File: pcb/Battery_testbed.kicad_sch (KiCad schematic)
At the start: 12 parts, among them U5 MIC5504-3.3YM5, U6 MCP73831-2-OT

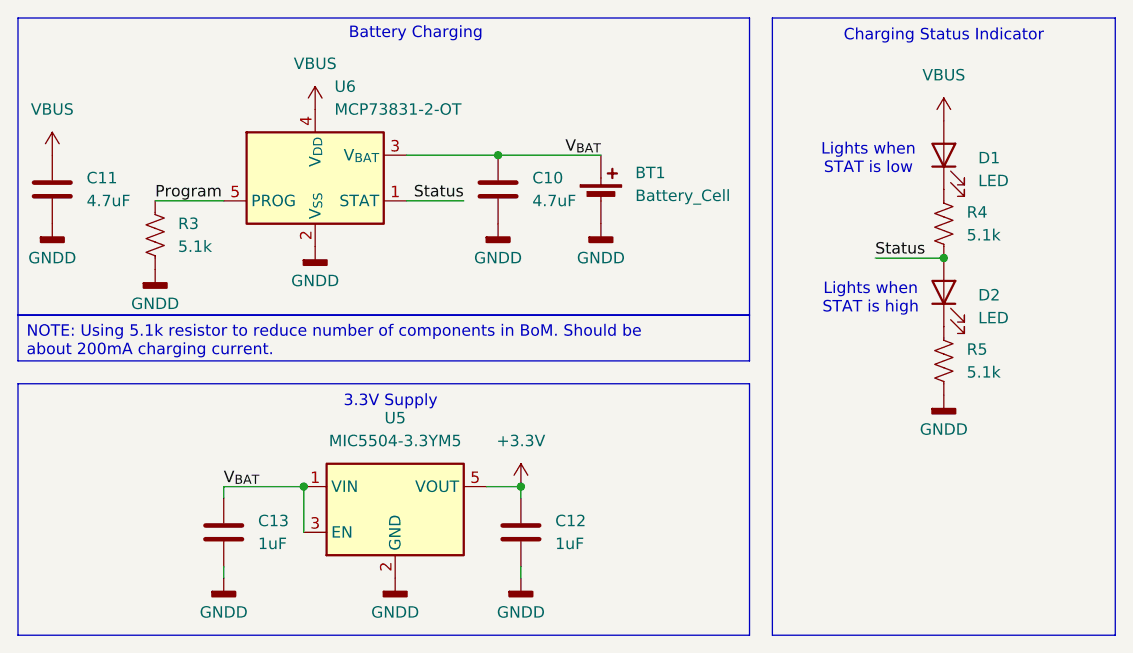
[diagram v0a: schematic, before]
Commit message: Updated Control Mod test bed schematics
finished testpoints, got rid of Vbus and replaced with +5V, added +3.3v to pyro J1 terminal
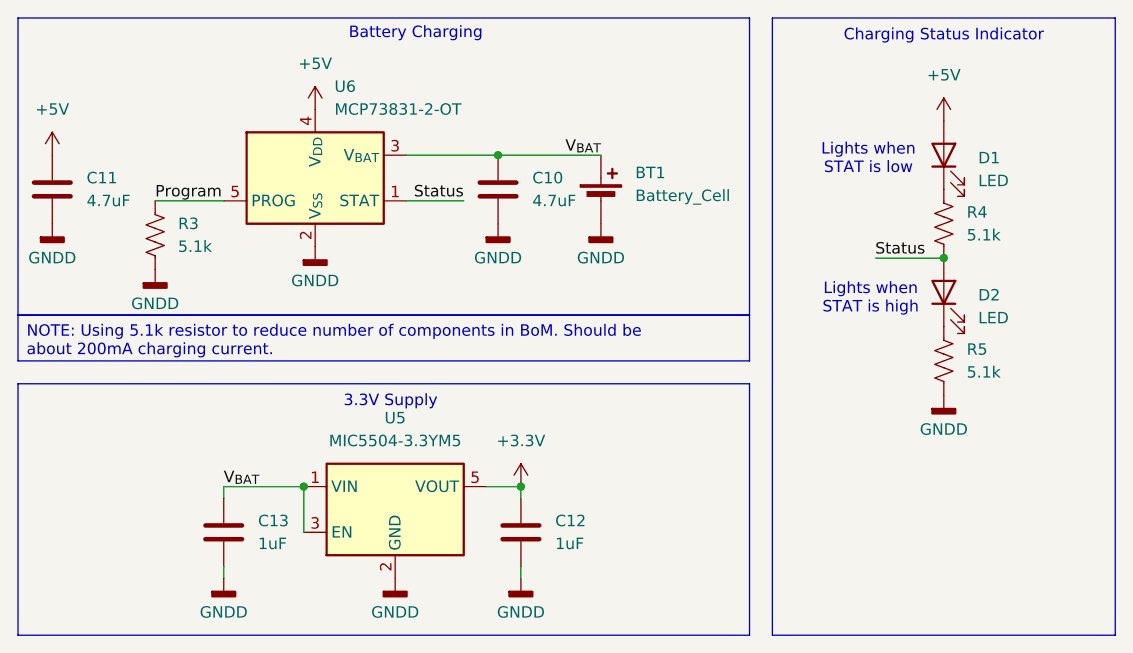
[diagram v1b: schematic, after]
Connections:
- net VBUS renamed +5V
